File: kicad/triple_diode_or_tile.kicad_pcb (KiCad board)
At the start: 2 copper layers, 24 x 24 mm, 8 parts, among them J1 input_1, J2 input_2, J3 input_3, J4 output_1

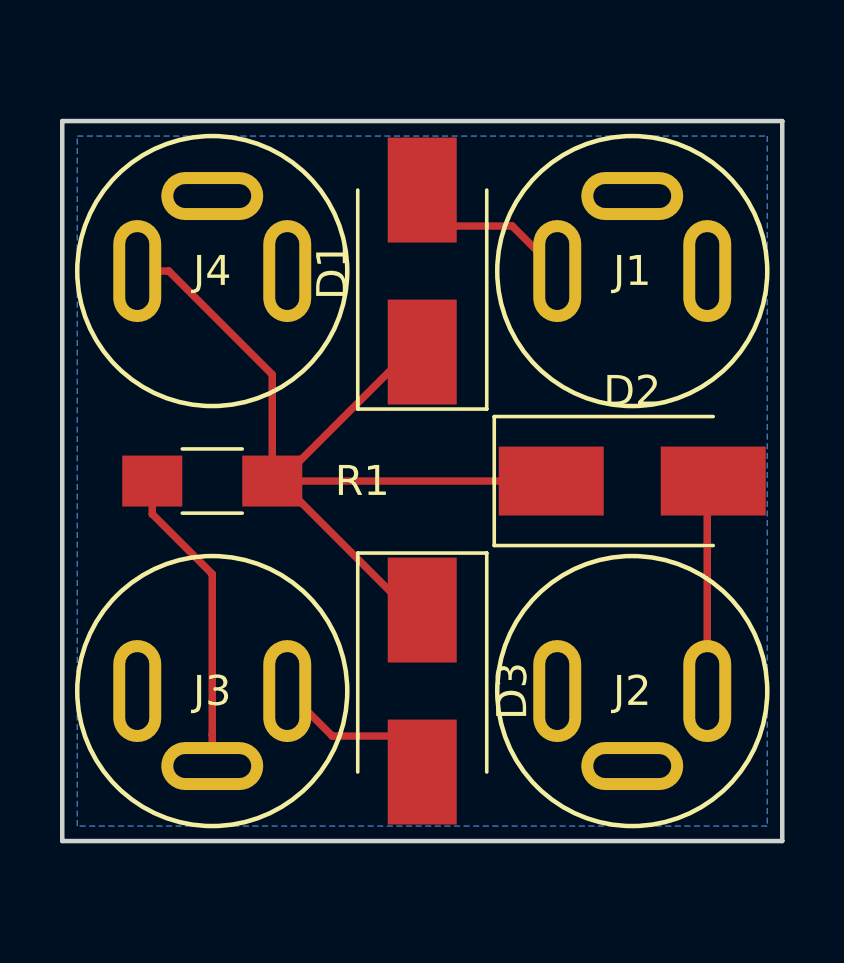
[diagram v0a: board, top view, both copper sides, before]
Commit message: Converted to kicad 6
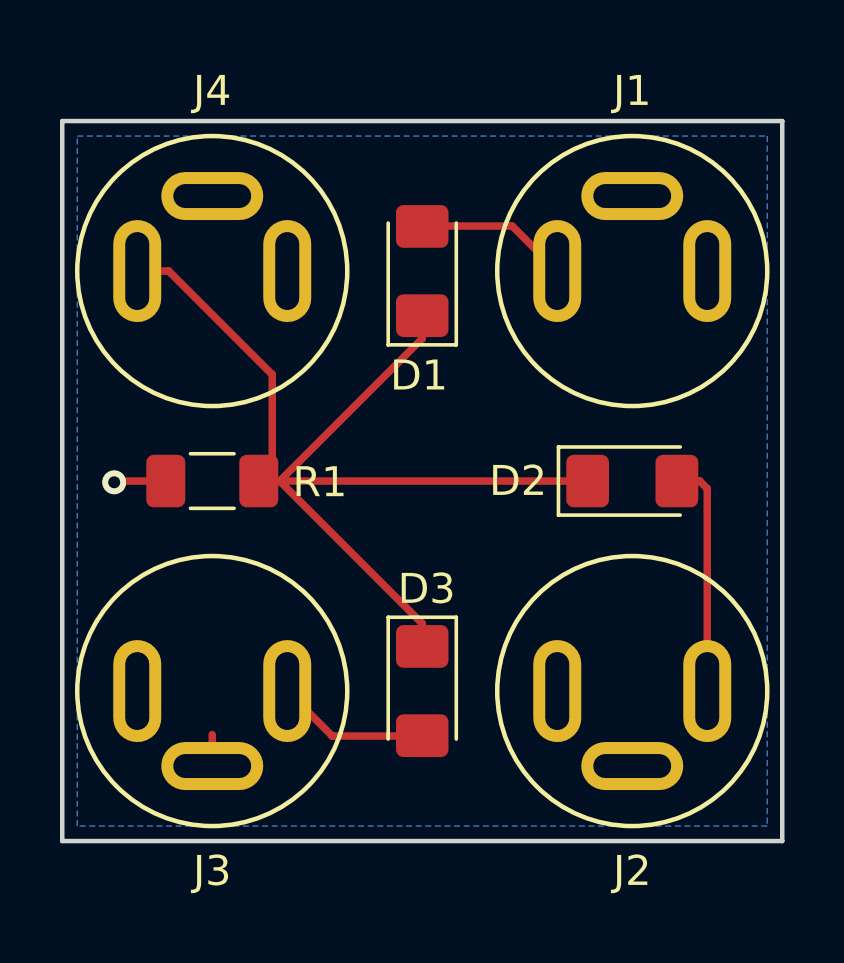
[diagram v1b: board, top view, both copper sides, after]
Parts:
- D1, D2, D3: footprint Diodes_SMD:D_SMB_Handsoldering -> Diode_SMD:D_1206_3216Metric_Pad1.42x1.75mm_HandSolder
- J1, J2, J3, J4: footprint eurorack:PJ392-3.5mm-jack-vertical-SRT -> OpenSoureModular:PJ392-3.5mm-jack-vertical-SRT
- R1: footprint Resistors_SMD:R_1206_HandSoldering -> Resistor_SMD:R_1206_3216Metric_Pad1.30x1.75mm_HandSolder
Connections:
- J1 pad R: Net-(J1-PadR) -> unconnected-(J1-PadR)
- J2 pad R: Net-(J2-PadR) -> unconnected-(J2-PadR)
- J3 pad R: Net-(J3-PadR) -> unconnected-(J3-PadR)
- J4 pad R: Net-(J4-PadR) -> unconnected-(J4-PadR)
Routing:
- net GND: track 10.3 -> 2.79 mm, vias 0 -> 1
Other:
- net class Default removed

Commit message: Minor updates as version 0.2. Added gerbers.
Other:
- rule pad_to_mask_clearance: 0.051 -> 0
- board text added: "Diode logic OR 0.2"
- board text removed: "Diode logic OR 0.1"
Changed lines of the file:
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@@
   )
   (setup
-    (pad_to_mask_clearance 0.051)
-    (solder_mask_min_width 0.25)
+    (stackup
+      (layer "F.SilkS" (type "Top Silk Screen"))
+      (layer "F.Paste" (type "Top Solder Paste"))
+      (layer "F.Mask" (type "Top Solder Mask") (thickness 0.01))
+      (layer "F.Cu" (type "copper") (thickness 0.035))
+      (layer "dielectric 1" (type "core") (thickness 1.51) (material "FR4") (epsilon_r 4.5) (loss_tangent 0.02))
+      (layer "B.Cu" (type "copper") (thickness 0.035))
+      (layer "B.Mask" (type "Bottom Solder Mask") (thickness 0.01))
+      (layer "B.Paste" (type "Bottom Solder Paste"))
+      (layer "B.SilkS" (type "Bottom Silk Screen"))
+      (copper_finish "None")
+      (dielectric_constraints no)
+    )
+    (pad_to_mask_clearance 0)
     (pcbplotparams
       (layerselection 0x00010fc_ffffffff)
@@
       (outputformat 1)
       (mirror false)
-      (drillshape 1)
+      (drillshape 0)
       (scaleselection 1)
-      (outputdirectory "")
+      (outputdirectory "../gerbers/")
     )
   )
@@
     (property "Sheetname" "")
     (attr through_hole)
-    (fp_text reference "J4" (at 0 -6) (layer "F.SilkS")
+    (fp_text reference "J4" (at 0 0) (layer "F.SilkS")
       (effects (font (size 1 1) (thickness 0.15)))
     )
@@
     (property "Sheetname" "")
     (attr through_hole)
-    (fp_text reference "J3" (at 0 -6 180) (layer "F.SilkS")
+    (fp_text reference "J3" (at 0 0 180) (layer "F.SilkS")
       (effects (font (size 1 1) (thickness 0.15)))
     )
@@
     (property "Sheetname" "")
     (attr through_hole)
-    (fp_text reference "J2" (at 0 -6 180) (layer "F.SilkS")
+    (fp_text reference "J2" (at 0 0 180) (layer "F.SilkS")
       (effects (font (size 1 1) (thickness 0.15)))
     )
@@
     (property "Sheetname" "")
     (attr through_hole)
-    (fp_text reference "J1" (at 0 -6) (layer "F.SilkS")
+    (fp_text reference "J1" (at 0 0) (layer "F.SilkS")
       (effects (font (size 1 1) (thickness 0.15)))
     )
@@
     (fp_line (start -1.6 0.8) (end -1.6 -0.8) (layer "F.Fab") (width 0.1))
     (fp_line (start 1.6 -0.8) (end 1.6 0.8) (layer "F.Fab") (width 0.1))
-    (pad "1" smd roundrect (at -1.55 0 180) (size 1.3 1.75) (layers "F.Cu" "F.Paste" "F.Mask") (roundrect_rratio 0.192308)
+    (pad "1" smd roundrect (at -1.55 0 180) (size 1.3 1.75) (layers "F.Cu" "F.Paste" "F.Mask") (roundrect_rratio 0.1923076923)
       (net 2 "Net-(D1-Pad1)") (pintype "passive"))
-    (pad "2" smd roundrect (at 1.55 0 180) (size 1.3 1.75) (layers "F.Cu" "F.Paste" "F.Mask") (roundrect_rratio 0.192308)
+    (pad "2" smd roundrect (at 1.55 0 180) (size 1.3 1.75) (layers "F.Cu" "F.Paste" "F.Mask") (roundrect_rratio 0.1923076923)
       (net 5 "GND") (pintype "passive"))
     (model "${KICAD6_3DMODEL_DIR}/Resistor_SMD.3dshapes/R_1206_3216Metric.wrl"
@@
     (fp_line (start -1.2 -0.8) (end -1.6 -0.4) (layer "F.Fab") (width 0.1))
     (fp_line (start 1.6 0.8) (end 1.6 -0.8) (layer "F.Fab") (width 0.1))
-    (pad "1" smd roundrect (at -1.4875 0 90) (size 1.425 1.75) (layers "F.Cu" "F.Paste" "F.Mask") (roundrect_rratio 0.175439)
+    (pad "1" smd roundrect (at -1.4875 0 90) (size 1.425 1.75) (layers "F.Cu" "F.Paste" "F.Mask") (roundrect_rratio 0.1754392982)
       (net 2 "Net-(D1-Pad1)") (pinfunction "K") (pintype "passive"))
-    (pad "2" smd roundrect (at 1.4875 0 90) (size 1.425 1.75) (layers "F.Cu" "F.Paste" "F.Mask") (roundrect_rratio 0.175439)
+    (pad "2" smd roundrect (at 1.4875 0 90) (size 1.425 1.75) (layers "F.Cu" "F.Paste" "F.Mask") (roundrect_rratio 0.1754392982)
       (net 1 "Net-(D1-Pad2)") (pinfunction "A") (pintype "passive"))
     (model "${KICAD6_3DMODEL_DIR}/Diode_SMD.3dshapes/D_1206_3216Metric.wrl"
@@
     (fp_line (start -1.2 -0.8) (end -1.6 -0.4) (layer "F.Fab") (width 0.1))
     (fp_line (start 1.6 -0.8) (end -1.2 -0.8) (layer "F.Fab") (width 0.1))
-    (pad "1" smd roundrect (at -1.4875 0) (size 1.425 1.75) (layers "F.Cu" "F.Paste" "F.Mask") (roundrect_rratio 0.175439)
+    (pad "1" smd roundrect (at -1.4875 0) (size 1.425 1.75) (layers "F.Cu" "F.Paste" "F.Mask") (roundrect_rratio 0.1754392982)
       (net 2 "Net-(D1-Pad1)") (pinfunction "K") (pintype "passive"))
-    (pad "2" smd roundrect (at 1.4875 0) (size 1.425 1.75) (layers "F.Cu" "F.Paste" "F.Mask") (roundrect_rratio 0.175439)
+    (pad "2" smd roundrect (at 1.4875 0) (size 1.425 1.75) (layers "F.Cu" "F.Paste" "F.Mask") (roundrect_rratio 0.1754392982)
       (net 3 "Net-(D2-Pad2)") (pinfunction "A") (pintype "passive"))
     (model "${KICAD6_3DMODEL_DIR}/Diode_SMD.3dshapes/D_1206_3216Metric.wrl"
@@
     (fp_line (start 1.6 -0.8) (end -1.2 -0.8) (layer "F.Fab") (width 0.1))
     (fp_line (start -1.6 0.8) (end 1.6 0.8) (layer "F.Fab") (width 0.1))
-    (pad "1" smd roundrect (at -1.4875 0 270) (size 1.425 1.75) (layers "F.Cu" "F.Paste" "F.Mask") (roundrect_rratio 0.175439)
+    (pad "1" smd roundrect (at -1.4875 0 270) (size 1.425 1.75) (layers "F.Cu" "F.Paste" "F.Mask") (roundrect_rratio 0.1754392982)
       (net 2 "Net-(D1-Pad1)") (pinfunction "K") (pintype "passive"))
-    (pad "2" smd roundrect (at 1.4875 0 270) (size 1.425 1.75) (layers "F.Cu" "F.Paste" "F.Mask") (roundrect_rratio 0.175439)
+    (pad "2" smd roundrect (at 1.4875 0 270) (size 1.425 1.75) (layers "F.Cu" "F.Paste" "F.Mask") (roundrect_rratio 0.1754392982)
       (net 4 "Net-(D3-Pad2)") (pinfunction "A") (pintype "passive"))
     (model "${KICAD6_3DMODEL_DIR}/Diode_SMD.3dshapes/D_1206_3216Metric.wrl"
@@
     (effects (font (size 1.5 1.5) (thickness 0.3)) (justify mirror))
   )
-  (gr_text "Diode logic OR 0.1" (at 152 82) (layer "B.SilkS")
+  (gr_text "Diode logic OR 0.2" (at 152 82) (layer "B.SilkS")
     (effects (font (size 1.5 1.5) (thickness 0.3)) (justify mirror))
   )
